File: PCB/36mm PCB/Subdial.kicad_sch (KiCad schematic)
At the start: 9 parts, among them Q3 2N7002KQBZ, Q4 2N7002KQBZ, Q5 2N7002KQBZ, Q6 2N7002KQBZ

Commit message: Modifs Mathieu
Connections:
- net +3.3V: now also Q3.3 (D_1), Q3.4 (D_2), Q4.3 (D_1), Q4.4 (D_2); no longer Q3.2 (S), Q4.2 (S), R14.1, R7.1
- net GND: now also Q5.1 (G), Q6.2 (S), R13.2, R8.2; no longer Q5.3 (D_1), Q5.4 (D_2), Q6.3 (D_1), Q6.4 (D_2)
- net H_Tim_1: now also R13.1, R7.1; no longer R13.2, R7.2
- net H_Tim_2: now also Q5.2 (S), R14.1, R8.1; no longer Q5.1 (G), R14.2, R8.2
- new net: L2.2, Q4.2 (S), Q6.3 (D_1), Q6.4 (D_2), R14.2
- new net: L2.1, Q3.2 (S), Q5.3 (D_1), Q5.4 (D_2), R7.2
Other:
- moved on the sheet: L2, Q4, Q5, R13, R14, R7, R8

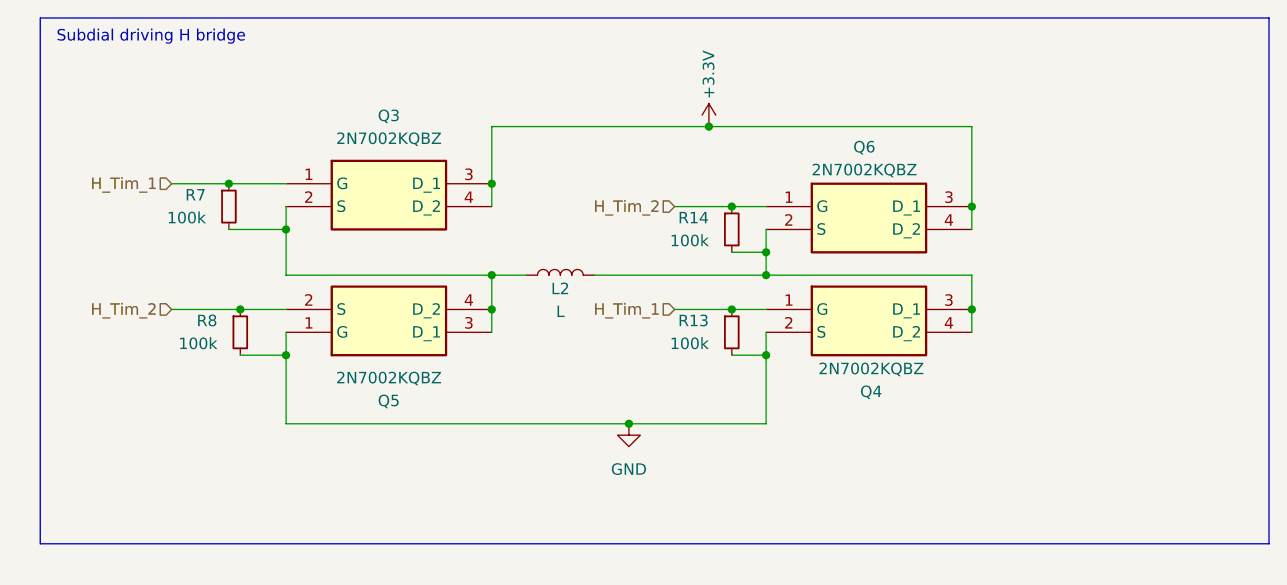
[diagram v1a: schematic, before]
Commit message: STM32 BLE + H chip
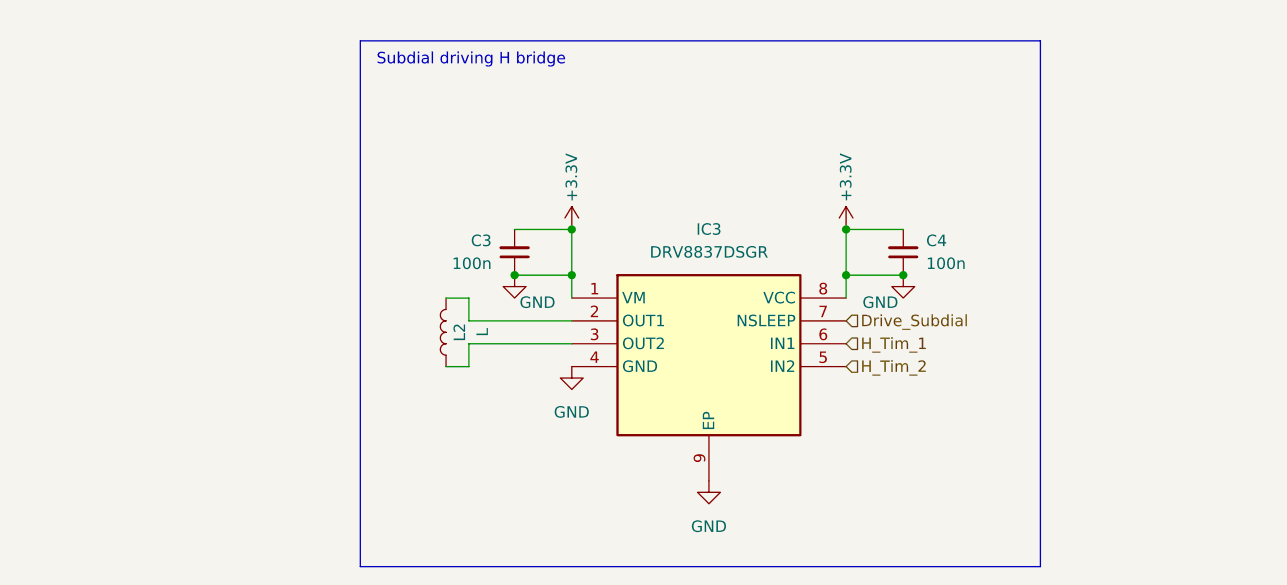
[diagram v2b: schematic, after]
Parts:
- removed Q3, Q4, Q5, Q6: 2N7002KQBZ, SamacSys_Parts:2N7002KQBZ, symbol SamacSys_Parts:2N7002KQBZ
- removed R13, R14, R7, R8: 100k, Resistor_SMD:R_0201_0603Metric, symbol Device:R_Small
- added C3, C4: 100n, Capacitor_SMD:C_0201_0603Metric, symbol Device:C_Small
- added IC3: DRV8837DSGR, SON50P200X200X80-9N, symbol SamacSys_Parts:DRV8837DSGR
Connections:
- net +3.3V: now also C3.1, C3.2, C4.1, C4.2, IC3.1 (VM), IC3.4 (GND), IC3.8 (VCC), IC3.9 (EP)
- net H_Tim_1: now also IC3.6 (IN1)
- net H_Tim_2: now also IC3.5 (IN2)
- net at L2.2: now also IC3.2 (OUT1)
- net at L2.1: now also IC3.3 (OUT2)
- new net Drive_Subdial: IC3.7 (NSLEEP)
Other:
- moved on the sheet: L2
